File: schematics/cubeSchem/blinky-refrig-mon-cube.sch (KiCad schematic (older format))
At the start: 23 parts, among them J1 VACout, J2 VACin, J3 CTin, J4 CTout, J5 Reed, J6 TripStatus, J7 SMA Ant, U2 ACS712_20, U3 FEATHER_M0_BASIC_PROTO, U4 AMAX31865

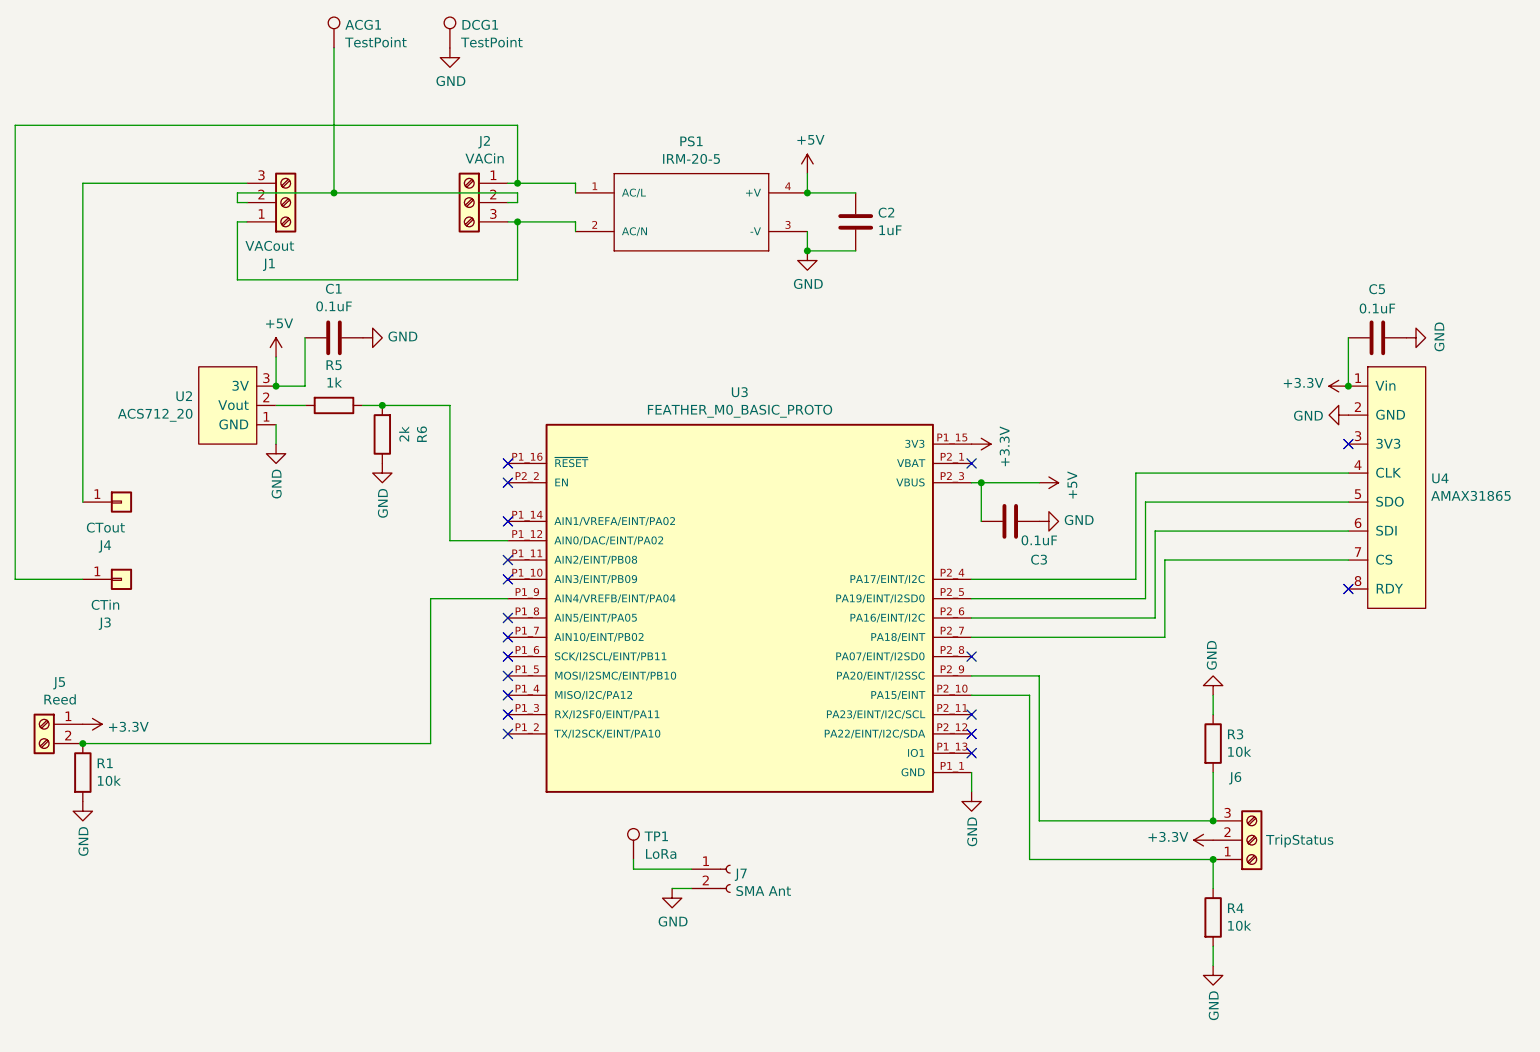
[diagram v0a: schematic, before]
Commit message: fixed lora footprint
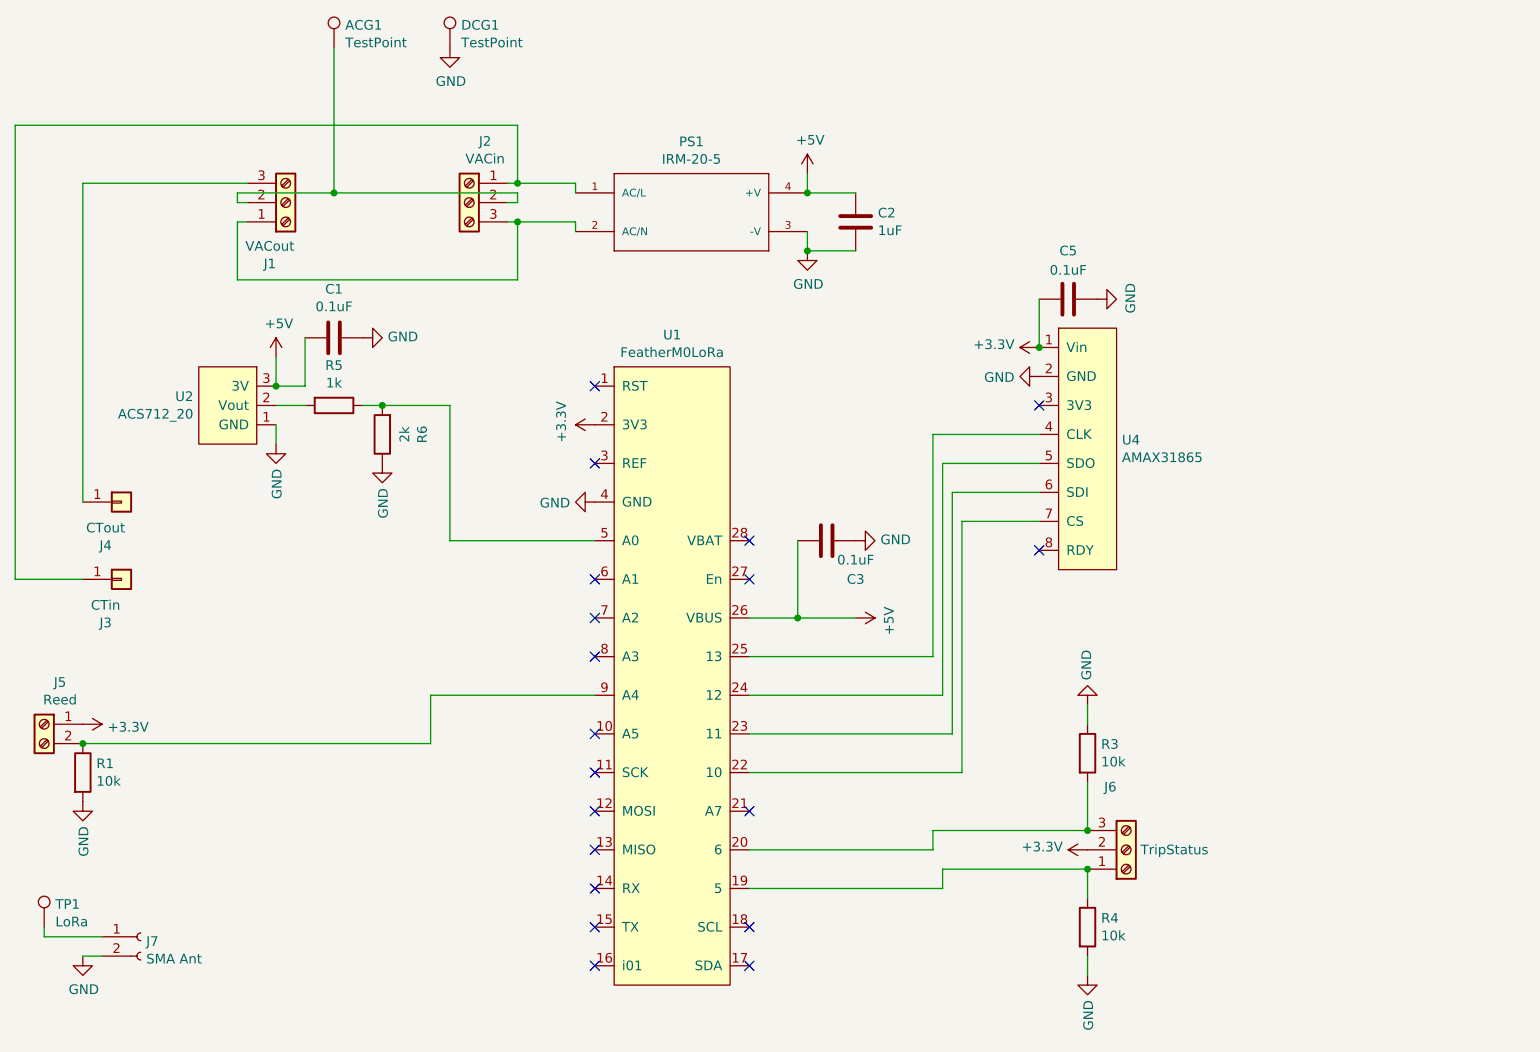
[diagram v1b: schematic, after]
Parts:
- removed U3: FEATHER_M0_BASIC_PROTO, FEATHER_M0_BASIC_PROTO:MODULE_FEATHER_M0_BASIC_PROTO, symbol FEATHER_M0_BASIC_PROTO:FEATHER_M0_BASIC_PROTO
- added U1: FeatherM0LoRa, dmcginnis427Footprints:FeatherM0LoRa, symbol dmcginnis427:FeatherM0LoRa
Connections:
- net +3V3: now also U1.2 (3V3)
- net +5V: now also U1.26 (VBUS)
- net GND: now also U1.4 (GND)
- net at R5.1, R6.2: now also U1.5 (A0)
- net at J5.2 (Pin_2), R1.1: now also U1.9 (A4)
- net at J6.1 (Pin_1), R4.1: now also U1.19 (5)
- net at U4.4 (CLK): now also U1.25 (13)
- net at U4.5 (SDO): now also U1.24 (12)
- net at U4.6 (SDI): now also U1.23 (11)
- net at U4.7 (CS): now also U1.22 (10)
- net at J6.3 (Pin_3), R3.2: now also U1.20 (6)
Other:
- moved on the sheet: C3, C5, J6, J7, R3, R4, TP1, U4
